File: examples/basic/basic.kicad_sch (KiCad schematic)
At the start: 4 parts

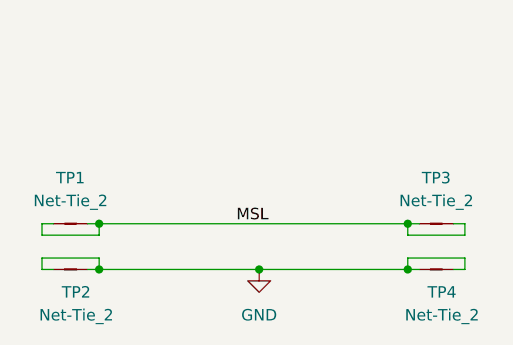
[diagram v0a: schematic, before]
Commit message: Proof of concept mods for modeling a resistor
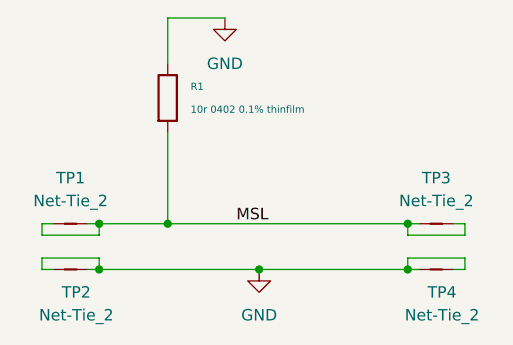
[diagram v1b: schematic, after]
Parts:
- added R1: 10r 0402 0.1% thinfilm, 1self_passives:R_0402_1005Metric, symbol 1self_passives2:R_10r_0402_0.1%_thinfilm
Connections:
- net GND: now also R1.2
- net MSL: now also R1.1
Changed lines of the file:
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@@
   (junction (at 156.21 101.6) (diameter 0) (color 0 0 0 0)
   )
+  (junction (at 129.54 96.52) (diameter 0) (color 0 0 0 0)
+  )
   (junction (at 121.92 101.6) (diameter 0) (color 0 0 0 0)
   )
@@
     (stroke (width 0) (type default))
   )
+  (wire (pts (xy 129.54 73.66) (xy 129.54 78.74))
+    (stroke (width 0) (type default))
+  )
   (wire (pts (xy 121.92 100.33) (xy 115.57 100.33))
     (stroke (width 0) (type default))
@@
     (stroke (width 0) (type default))
   )
+  (wire (pts (xy 129.54 86.36) (xy 129.54 96.52))
+    (stroke (width 0) (type default))
+  )
   (wire (pts (xy 162.56 101.6) (xy 162.56 100.33))
     (stroke (width 0) (type default))
   )
+  (wire (pts (xy 135.89 73.66) (xy 129.54 73.66))
+    (stroke (width 0) (type default))
+  )
   (wire (pts (xy 121.92 101.6) (xy 121.92 100.33))
     (stroke (width 0) (type default))
@@
     (stroke (width 0) (type default))
   )
+  (wire (pts (xy 129.54 96.52) (xy 156.21 96.52))
+    (stroke (width 0) (type default))
+  )
   (wire (pts (xy 139.7 101.6) (xy 156.21 101.6))
     (stroke (width 0) (type default))
@@
     (stroke (width 0) (type default))
   )
-  (wire (pts (xy 121.92 96.52) (xy 156.21 96.52))
+  (wire (pts (xy 121.92 96.52) (xy 129.54 96.52))
     (stroke (width 0) (type default))
   )
@@
     )
   )
+  (symbol (lib_id "antmicropower:GND") (at 135.89 73.66 0) (unit 1)
+    (in_bom yes) (on_board yes) (dnp no) (fields_autoplaced)
+    (property "Reference" "#PWR01" (at 144.78 76.2 0)
+      (effects (font (size 1.27 1.27) (thickness 0.15)) (justify left bottom) hide)
+    )
+    (property "Value" "GND" (at 135.89 78.74 0)
+      (effects (font (size 1.27 1.27) (thickness 0.15)))
+    )
+    (property "Footprint" "" (at 144.78 81.28 0)
+      (effects (font (size 1.27 1.27) (thickness 0.15)) (justify left bottom) hide)
+    )
+    (property "Datasheet" "" (at 144.78 86.36 0)
+      (effects (font (size 1.27 1.27) (thickness 0.15)) (justify left bottom) hide)
+    )
+    (property "Author" "Antmicro" (at 144.78 81.28 0)
+      (effects (font (size 1.27 1.27) (thickness 0.15)) (justify left bottom) hide)
+    )
+    (property "License" "Apache-2.0" (at 144.78 83.82 0)
+      (effects (font (size 1.27 1.27) (thickness 0.15)) (justify left bottom) hide)
+    )
+    (pin "1")
+    (instances
+      (project "basic"
+        (path "/fb78e210-299c-4ada-a64d-208900768eb0"
+          (reference "#PWR01") (unit 1)
+        )
+      )
+    )
+  )
   (symbol (lib_id "antmicropower:GND") (at 139.7 101.6 0) (unit 1)
     (in_bom yes) (on_board yes) (dnp no) (fields_autoplaced)
@@
         )
       )
+    )
+  )
+  (symbol (lib_id "1self_passives2:R_10r_0402_0.1%_thinfilm") (at 129.54 82.55 90) (unit 1)
+    (in_bom yes) (on_board yes) (dnp no) (fields_autoplaced)
+    (property "Reference" "R1" (at 132.08 81.28 90)
+      (effects (font (size 0.8 0.8)) (justify right))
+    )
+    (property "Value" "10r 0402 0.1% thinfilm" (at 132.08 83.82 90)
+      (effects (font (size 0.8 0.8)) (justify right))
+    )
+    (property "Footprint" "1self_passives:R_0402_1005Metric" (at 121.92 74.93 0)
+      (effects (font (size 0.8 0.8)) hide)
+    )
+    (property "Datasheet" "https://www.te.com/commerce/DocumentDelivery/DDEController?Action=srchrtrv&DocNm=1773200&DocType=DS&DocLang=English" (at 121.92 76.2 0)
+      (effects (font (size 0.8 0.8)) hide)
+    )
+    (property "similar_resistors" " " (at 110.49 59.69 0)
+      (effects (font (size 0.8 0.8)) hide)
+    )
+    (property "AVR" "TE Connectivity Passive Product" (at 120.65 73.66 0)
+      (effects (font (size 0.8 0.8)) hide)
+    )
+    (property "Mfg Part #" "CPF0402B10RE1" (at 123.19 72.39 0)
+      (effects (font (size 0.8 0.8)) hide)
+    )
+    (property "Description" "RES SMD 10 OHM 0.1% 1/16W 0402 " (at 120.65 69.85 0)
+      (effects (font (size 0.8 0.8)) hide)
+    )
+    (property "Detailed Description" "10 Ohms ±0.1% 0.063W, 1/16W Chip Resistor 0402 (1005 Metric)  Thin Film" (at 113.03 67.31 0)
+      (effects (font (size 0.8 0.8)) hide)
+    )
+    (property "size(LWT,mm)" "1x0.5x0.35" (at 115.57 64.77 0)
+      (effects (font (size 0.8 0.8)) hide)
+    )
+    (pin "2")
+    (pin "1")
+    (instances
+      (project "basic"
+        (path "/fb78e210-299c-4ada-a64d-208900768eb0"
+          (reference "R1") (unit 1)
+        )
+      )
